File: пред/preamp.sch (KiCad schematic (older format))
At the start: 48 parts

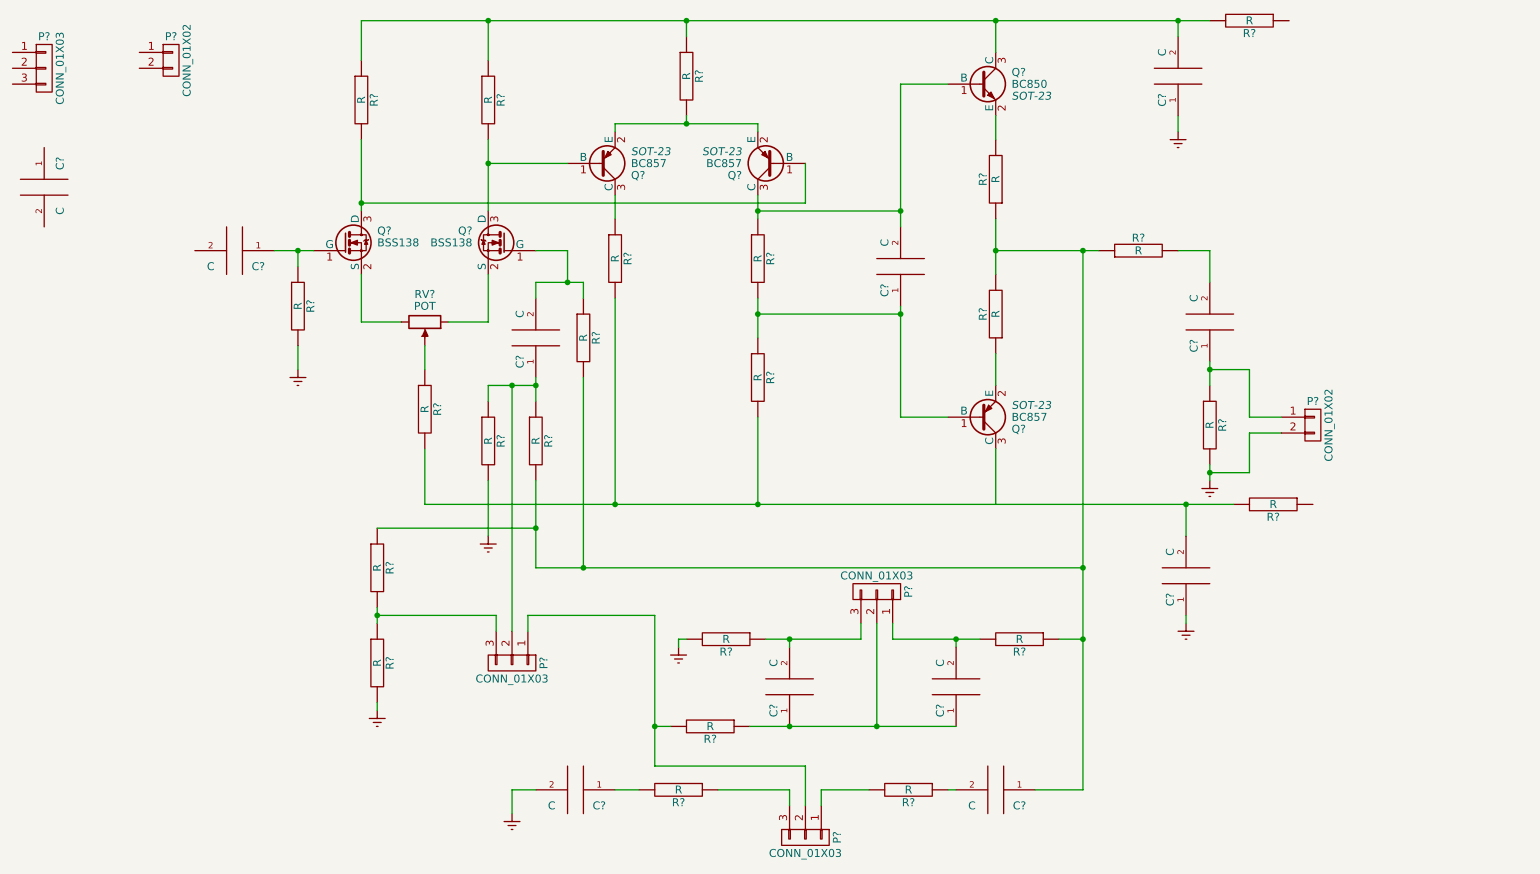
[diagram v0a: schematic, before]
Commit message: Создана печатная плата, назначены посадочные места
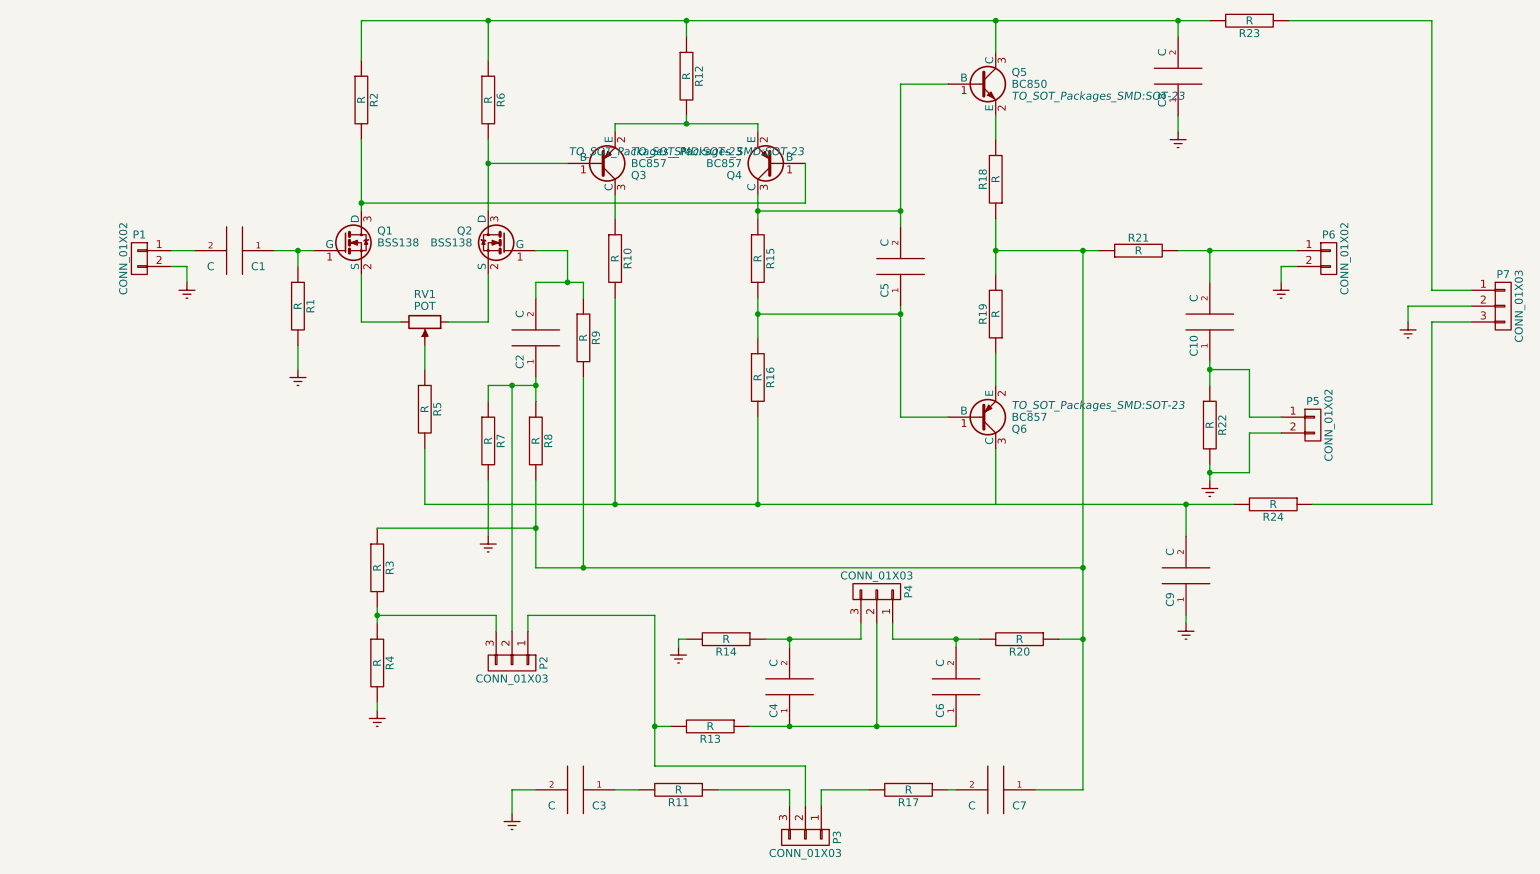
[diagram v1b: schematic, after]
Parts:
- removed C?: C, symbol C
- removed P?: CONN_01X03, symbol CONN_01X03
- added P6: CONN_01X02, Pin_Headers:Pin_Header_Angled_1x02_Pitch2.54mm, symbol CONN_01X02
- added P7: CONN_01X03, Pin_Headers:Pin_Header_Straight_1x03_Pitch2.54mm, symbol CONN_01X03
- C1, C10, C2, C3, C4, C5, C6, C7: renamed from C?; footprint (none) -> Capacitors_SMD:C_0805
- C8, C9: renamed from C?; footprint (none) -> Capacitors_THT:CP_Radial_D8.0mm_P3.50mm
- P1, P5: renamed from P?; footprint (none) -> Pin_Headers:Pin_Header_Angled_1x02_Pitch2.54mm
- P2, P3, P4: renamed from P?; footprint (none) -> Pin_Headers:Pin_Header_Straight_1x03_Pitch2.54mm
- Q3, Q4, Q5, Q6: renamed from Q?; footprint SOT-23 -> TO_SOT_Packages_SMD:SOT-23
- R1, R10, R11, R12, R13, R14, R15, R16, R17, R18, R19, R2, R20, R21, R22, R23, R24, R3, R4, R5, R6, R7, R8, R9: renamed from R?; footprint (none) -> Resistors_SMD:R_1206
- RV1: renamed from RV?; footprint (none) -> Potentiometers:Potentiometer_Trimmer_Bourns_3299W
- gave numbers to parts that had none: 2
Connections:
- net GNDREF: now also P1.2 (P2), P6.2 (P2), P7.2 (P2)
- net at P1.1 (P1): now also C1.2
- net at C10.2, R21.2: now also P6.1 (P1)
- net at R24.1: now also P7.3 (P3)
- net at R23.1: now also P7.1 (P1)
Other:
- moved on the sheet: P1

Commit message: Начата трассировка
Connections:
- net at C9.2, R10.2, R16.2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: now also Q6.3 (C)
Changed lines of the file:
@@
 	5100 2400 5100 3700
-Wire Wire Line
-	3900 3700 9000 3700
 Wire Wire Line
 	3900 3700 3900 3350
@@
 	7500 650  7500 850
 Connection ~ 5550 650
-Wire Wire Line
-	7500 3350 7500 3700
 Connection ~ 6000 3700
 Wire Wire Line
@@
 	9300 2200 9400 2200
 Connection ~ 8850 2100
+Wire Wire Line
+	3900 3700 9000 3700
+Wire Wire Line
+	7500 3350 7500 3700
+Connection ~ 7500 3700
 $EndSCHEMATC
